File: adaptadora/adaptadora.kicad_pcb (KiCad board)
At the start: 2 copper layers, 105 parts, among them J1 Conn_Coaxial, J10 Conn_Coaxial, J11 Conn_Coaxial, J12 Conn_Coaxial, J13 Conn_Coaxial, J14 Conn_Coaxial, J15 Conn_Coaxial, J16 Conn_Coaxial, J17 Conn_Coaxial, J18 Conn_Coaxial, J19 Conn_Coaxial, J2 Conn_Coaxial, J20 Conn_Coaxial, J21 Conn_Coaxial, J22 Conn_Coaxial, J23 Conn_Coaxial, J3 Conn_Coaxial, J4 Conn_Coaxial, J5 Conn_02x20_Odd_Even, J6 Conn_01x02, J7 Conn_02x20_Odd_Even, J8 Conn_01x04, J9 Conn_01x02, U11 LM361MX_NOPB, U12 LM361MX_NOPB, U13 LM361MX_NOPB, U14 LM361MX_NOPB, U21 TLV2772IDR, U22 TLV2772IDR, U23 TLV2772IDR, U24 TLV2772IDR, U25 TLV2772IDR, U31 SN74LVC2T45DCUR, U32 SN74LVC2T45DCUR

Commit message: Componentes acomodados en PCB
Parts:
- U11, U12, U13, U14: footprint Package_DIP:DIP-14_W7.62mm -> Package_SO:SOIC-14_3.9x8.7mm_P1.27mm
- U21: footprint Package_SO:SOIC-8_7.5x5.85mm_P1.27mm -> Package_SO:SOIC-8_3.9x4.9mm_P1.27mm; moved to F.Cu
- U22, U23, U24, U25: footprint Package_SO:SOIC-8_7.5x5.85mm_P1.27mm -> Package_SO:SOIC-8_3.9x4.9mm_P1.27mm
- moved TP1 216.2 mm to (44.5, 81.3)
- moved C16 211.8 mm to (39.4, 85.1)
- moved J12 211.8 mm to (49.5, 29.2)
- moved C12 208.2 mm to (54.6, 63.2), turned to 270 degrees
- moved C8 206.9 mm to (36.8, 59.7), turned to 90 degrees
- moved C14 206.2 mm to (36.8, 68.6), turned to 270 degrees
- moved R5 206.1 mm to (47.0, 59.7), turned to 90 degrees
- moved C19 200.7 mm to (57.1, 92.7), turned to 270 degrees
- moved JP3 195.9 mm to (50.8, 39.4)
- moved J14 194.8 mm to (34.3, 102.9)
- moved JP5 194.8 mm to (44.5, 74.9), turned to 180 degrees
- moved C18 192.2 mm to (69.8, 92.7), turned to 90 degrees
- moved J16 189.1 mm to (49.5, 102.9)
- moved C10 188.5 mm to (54.6, 68.6), turned to 270 degrees
- moved R1 188.1 mm to (223.5, 40.6), turned to 90 degrees
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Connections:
- J5 pad 12: Net-(J5-Pad12) -> GND
- J5 pad 30: Net-(J5-Pad30) -> GND

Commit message: Se dibuja borde de placa
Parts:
- moved J10 134.3 mm to (91.4, 133.3)
- moved C1 133.1 mm to (95.2, 123.2)
- moved U25 131.5 mm to (87.6, 123.2)
- moved J11 106.1 mm to (105.4, 133.3)
- moved J2 103.5 mm to (233.7, 132.1), turned to 180 degrees
- moved R2 85.9 mm to (222.2, 119.4), turned to 270 degrees
- moved JP2 85.0 mm to (232.4, 124.5), turned to 180 degrees
- moved J6 76.3 mm to (138.4, 100.3)
- moved RV2 70.8 mm to (233.7, 118.1), turned to 180 degrees
- moved D2 49.9 mm to (236.2, 110.5), turned to 0 degrees
- moved C16 44.6 mm to (81.3, 100.3)
- moved J14 43.8 mm to (76.2, 115.6)
- moved J9 40.2 mm to (58.4, 104.1)
- moved C4 37.9 mm to (77.5, 129.5)
- moved C6 37.9 mm to (78.7, 135.9)
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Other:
- board outline added: 199.4 x 99.1 mm

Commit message: correcciones y archivos agregados
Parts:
- D1, D2, D3, D4, D5, D6: footprint Diode_THT:D_DO-15_P10.16mm_Horizontal -> Diode_SMD:D_0201_0603Metric
- moved C30 12.0 mm to (184.2, 108.0)
- moved C31 12.0 mm to (171.4, 108.0)
- moved U32 12.0 mm to (177.8, 108.0)
- moved U31 10.5 mm to (91.4, 108.0)
- moved C18 10.5 mm to (97.8, 108.0)
- moved C19 10.5 mm to (85.1, 108.0)
- moved C10 3.81 mm to (81.3, 82.5)
- moved C11 3.81 mm to (124.5, 82.5)
- moved C12 3.81 mm to (81.3, 77.1)
- moved C13 3.81 mm to (124.5, 77.5)
- moved C14 3.81 mm to (63.5, 82.5)
- moved C15 3.81 mm to (108.0, 82.5)
- moved C16 3.81 mm to (81.3, 96.5)
- moved C17 3.81 mm to (124.5, 96.5)
- moved C20 3.81 mm to (149.9, 73.7)
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
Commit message: pcb, work in progress
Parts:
- removed C29: 0.1uF-50V, Capacitor_SMD:C_0805_2012Metric
- removed J21, J23: Conn_Coaxial, Connector_Coaxial:SMA_Amphenol_901-144_Vertical
- removed U24: TLV2772IDR, Package_SO:SOIC-8_3.9x4.9mm_P1.27mm
- moved J10 110.7 mm to (200.4, 114.0), turned to 90 degrees
- moved J7 106.5 mm to (108.0, 135.9)
- moved U25 101.6 mm to (189.0, 116.9), turned to 90 degrees
- moved J11 100.5 mm to (205.7, 127.0), turned to 90 degrees
- moved C1 95.8 mm to (190.3, 110.6)
- moved C6 81.8 mm to (61.0, 56.0), turned to 0 degrees
- moved C7 79.9 mm to (61.0, 60.0), turned to 0 degrees
- moved C4 78.5 mm to (60.0, 53.0), turned to 0 degrees
- moved J8 76.7 mm to (53.0, 57.0), turned to 0 degrees
- moved C5 75.5 mm to (61.0, 63.0), turned to 0 degrees
- moved C2 73.4 mm to (61.0, 65.0), turned to 0 degrees
- moved C3 71.9 mm to (61.0, 67.9), turned to 180 degrees
- moved J6 61.9 mm to (189.2, 135.9), turned to 270 degrees
- moved C19 11.4 mm to (88.9, 97.2)
- moved U31 11.4 mm to (95.2, 97.2)
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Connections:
- C14 pad 1: -12V -> GND
- C14 pad 2: GND -> -12V
- C15 pad 1: -12V -> GND
- C15 pad 2: GND -> -12V
- C2 pad 1: -12V -> GND
- C2 pad 2: GND -> -12V
- C26 pad 1: -12V -> GND
- C26 pad 2: GND -> -12V
- C27 pad 1: -12V -> GND
- C27 pad 2: GND -> -12V
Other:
- board size 199.4 x 99.1 mm -> 200 x 100 mm
- board text added: "+12V"
- board text added: "+3.3V"
- board text added: "-12V"
- board text added: "5V"
- board text added: "ACP"
- board text added: "ACP OUT (5V)"
- board text added: "ARP"
- board text added: "ARP OUT (3.3V)"
- board text added: "ARP OUT (5V)"
- board text added: "DAC"
- board text added: "GND"
- board text added: "GPIO 2 X 20 (ADC/SoC)"
- board text added: "PRF"
- board text added: "PRF OUT (5V)"
- board text added: "Placa Adaptadora de Señales de Radar Diseño de Circuitos Impresos Especialización en Sistemas Embebidos Noviembre 2019"
- board text added: "SECUNDARIO"
- board text added: "VIDEO 1 IN"
- board text added: "VIDEO 2 IN"
- board text added: "VIDEO OUT (5V)"
- board text added: "VIDEO OUT ADC IN"

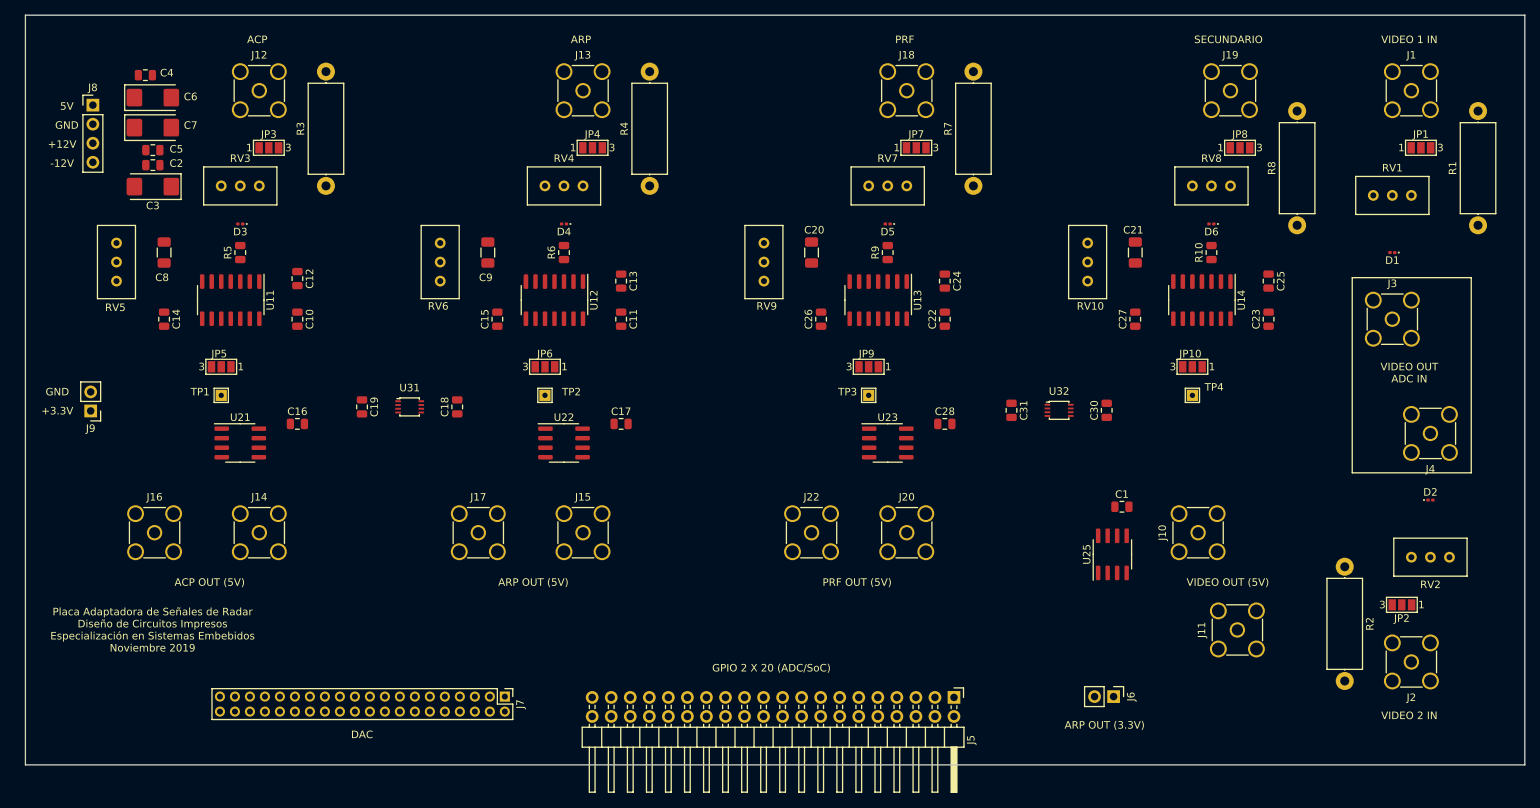
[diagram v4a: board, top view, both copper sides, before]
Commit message: pcb en proceso de diseño
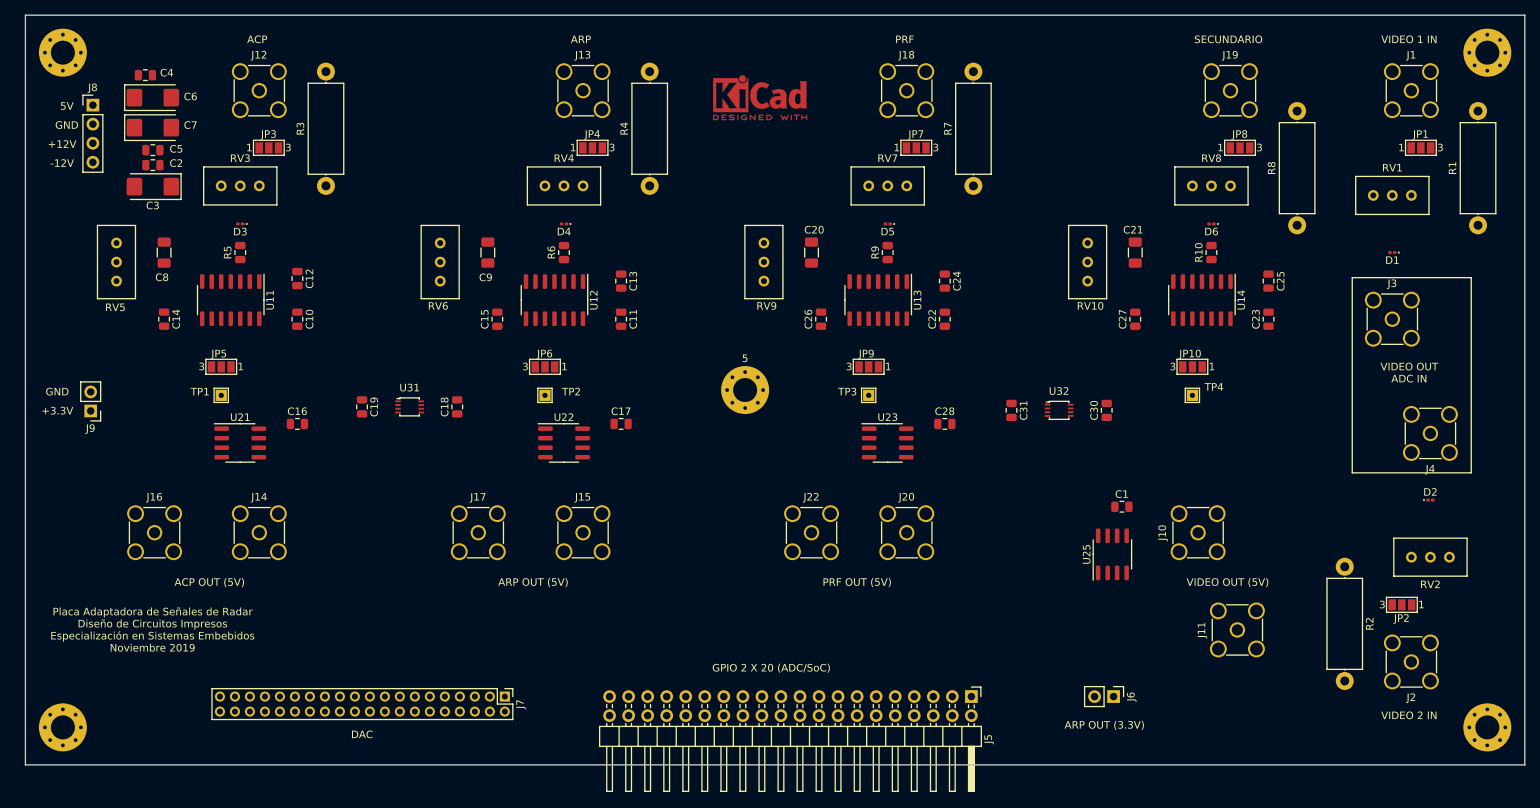
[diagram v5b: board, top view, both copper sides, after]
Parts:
- added 1: MountingHole_3.2mm_M3_Pad_Via, MountingHole:MountingHole_3.2mm_M3_Pad_Via, F.Cu at (49.0, 50.0)
- added 2: MountingHole_3.2mm_M3_Pad_Via, MountingHole:MountingHole_3.2mm_M3_Pad_Via, F.Cu at (239.0, 50.0)
- added 3: MountingHole_3.2mm_M3_Pad_Via, MountingHole:MountingHole_3.2mm_M3_Pad_Via, F.Cu at (239.0, 140.0)
- added 4: MountingHole_3.2mm_M3_Pad_Via, MountingHole:MountingHole_3.2mm_M3_Pad_Via, F.Cu at (49.0, 140.0)
- added 5: MountingHole_3.2mm_M3_Pad_Via, MountingHole:MountingHole_3.2mm_M3_Pad_Via, F.Cu at (140.0, 95.0)
- added REF**: KiCad-Logo2_5mm_Copper, Symbol:KiCad-Logo2_5mm_Copper, F.Cu at (142.0, 56.0)
- moved J5 2.32 mm to (170.2, 135.9)

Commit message: esq y pcb work in progress
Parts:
- removed 1, 2, 3, 4, 5: MountingHole_3.2mm_M3_Pad_Via, MountingHole:MountingHole_3.2mm_M3_Pad_Via
- added H1: MountingHole, MountingHole:MountingHole_3.2mm_M3_Pad, F.Cu at (49.0, 140.0)
- added H2: MountingHole, MountingHole:MountingHole_3.2mm_M3_Pad, F.Cu at (49.0, 50.0)
- added H3: MountingHole, MountingHole:MountingHole_3.2mm_M3_Pad, F.Cu at (239.0, 50.0)
- added H4: MountingHole, MountingHole:MountingHole_3.2mm_M3_Pad, F.Cu at (239.0, 140.0)
- added H5: MountingHole, MountingHole:MountingHole_3.2mm_M3_Pad, F.Cu at (140.0, 95.0)
